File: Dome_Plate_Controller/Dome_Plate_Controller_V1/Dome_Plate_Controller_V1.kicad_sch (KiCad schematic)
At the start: 35 parts, among them J1 USB_B_Micro, J10 SERIAL_FU4, J11 SERIAL_FU3, J12 SERIAL_FU, J13 DB25_Female_MountingHoles, J14 DC-005-5A-2.0, J15 SERIAL_FU2, J2 DB25_Female_MountingHoles, J3 12VOUT, J4 SERIAL_RS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

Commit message: Working on new body control board
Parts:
- J13: value DB25_Female_MountingHoles -> DB25_Female_MagTag; LCSC C77833 -> C2834383
- J2: value DB25_Female_MountingHoles -> DB25_Male_SlipRing; footprint Connector_Dsub:DSUB-25_Female_Vertical_P2.77x2.84mm_MountingHoles -> Connector_Dsub:DSUB-25_Male_Vertical_P2.77x2.84mm_MountingHoles; LCSC C77833 -> C2834344
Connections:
- net RX_FU2: no longer U1.9 (IO33)
- net TX_FU2: no longer U1.8 (IO32)
- no-connect marks 30 -> 32
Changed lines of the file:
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@@
   (no_connect (at 69.85 73.66))
   (no_connect (at 87.63 187.96))
+  (no_connect (at 52.07 55.88))
   (no_connect (at 54.61 186.69))
   (no_connect (at 166.37 93.98))
@@
   (no_connect (at 95.25 53.34))
   (no_connect (at 135.89 97.79))
+  (no_connect (at 52.07 53.34))
   (no_connect (at 72.39 73.66))
   (no_connect (at 46.99 151.13))
@@
     )
   )
-  (global_label "TX_FU2" (shape input) (at 52.07 53.34 180) (fields_autoplaced)
-    (effects (font (size 1.27 1.27)) (justify right))
-    (property "Intersheet References" "${INTERSHEET_REFS}" (id 0) (at 42.8836 53.2606 0)
-      (effects (font (size 1.27 1.27)) (justify right) hide)
-    )
-  )
   (global_label "D+" (shape input) (at 135.89 92.71 0) (fields_autoplaced)
     (effects (font (size 1.27 1.27)) (justify left))
@@
     )
   )
-  (global_label "RX_FU2" (shape input) (at 96.52 78.74 0) (fields_autoplaced)
-    (effects (font (size 1.27 1.27)) (justify left))
-    (property "Intersheet References" "${INTERSHEET_REFS}" (id 0) (at 106.0088 78.6606 0)
-      (effects (font (size 1.27 1.27)) (justify left) hide)
-    )
-  )
   (global_label "RXD0" (shape input) (at 95.25 45.72 0) (fields_autoplaced)
     (effects (font (size 1.27 1.27)) (justify left))
@@
     (effects (font (size 1.27 1.27)) (justify right))
     (property "Intersheet References" "${INTERSHEET_REFS}" (id 0) (at 31.6706 101.4447 90)
-      (effects (font (size 1.27 1.27)) (justify right) hide)
-    )
-  )
-  (global_label "RX_FU2" (shape input) (at 52.07 55.88 180) (fields_autoplaced)
-    (effects (font (size 1.27 1.27)) (justify right))
-    (property "Intersheet References" "${INTERSHEET_REFS}" (id 0) (at 42.5812 55.8006 0)
       (effects (font (size 1.27 1.27)) (justify right) hide)
     )
@@
       (effects (font (size 1.27 1.27)) (justify left))
     )
-    (property "Value" "DB25_Female_MountingHoles" (id 1) (at 38.1 190.4999 0)
+    (property "Value" "DB25_Female_MagTag" (id 1) (at 38.1 190.4999 0)
       (effects (font (size 1.27 1.27)) (justify left))
     )
@@
       (effects (font (size 1.27 1.27)) hide)
     )
-    (property "LCSC" "C77833" (id 4) (at 54.61 151.13 0)
+    (property "LCSC" "C2834383" (id 4) (at 54.61 151.13 0)
       (effects (font (size 1.27 1.27)) hide)
     )
@@
       (effects (font (size 1.27 1.27)) (justify left))
     )
-    (property "Value" "DB25_Female_MountingHoles" (id 1) (at 73.66 191.7699 0)
-      (effects (font (size 1.27 1.27)) (justify left))
-    )
-    (property "Footprint" "Connector_Dsub:DSUB-25_Female_Vertical_P2.77x2.84mm_MountingHoles" (id 2) (at 87.63 152.4 0)
+    (property "Value" "DB25_Male_SlipRing" (id 1) (at 73.66 191.7699 0)
+      (effects (font (size 1.27 1.27)) (justify left))
+    )
+    (property "Footprint" "Connector_Dsub:DSUB-25_Male_Vertical_P2.77x2.84mm_MountingHoles" (id 2) (at 87.63 152.4 0)
       (effects (font (size 1.27 1.27)) hide)
     )
@@
       (effects (font (size 1.27 1.27)) hide)
     )
-    (property "LCSC" "C77833" (id 4) (at 87.63 152.4 0)
+    (property "LCSC" "C2834344" (id 4) (at 87.63 152.4 0)
       (effects (font (size 1.27 1.27)) hide)
     )
@@
     )
     (path "/6bc43df8-b439-4c10-945f-79b8aa8b1bbf"
-      (reference "J2") (unit 1) (value "DB25_Female_MountingHoles") (footprint "Connector_Dsub:DSUB-25_Female_Vertical_P2.77x2.84mm_MountingHoles")
+      (reference "J2") (unit 1) (value "DB25_Male_SlipRing") (footprint "Connector_Dsub:DSUB-25_Male_Vertical_P2.77x2.84mm_MountingHoles")
     )
     (path "/6e24a65e-6cc3-44ac-8a5b-662642e9396d"
@@
     )
     (path "/1eb3ffea-e932-409f-b4af-7d3f3af9d359"
-      (reference "J13") (unit 1) (value "DB25_Female_MountingHoles") (footprint "Connector_Dsub:DSUB-25_Female_Vertical_P2.77x2.84mm_MountingHoles")
+      (reference "J13") (unit 1) (value "DB25_Female_MagTag") (footprint "Connector_Dsub:DSUB-25_Female_Vertical_P2.77x2.84mm_MountingHoles")
     )
     (path "/b42cd28b-6776-49c3-af7d-a30bc22f7b3a"

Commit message: Added a lot since last check in
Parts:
- J4: value SERIAL_RS -> SERIAL_US
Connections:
- net D+: no longer J13.9
- net D-: no longer J13.21 (P21)
- net GND: no longer J13.8
- net VBUS: no longer J13.20 (P20)
- no-connect marks 32 -> 36
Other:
- moved on the sheet: J10, J11, J12, J15

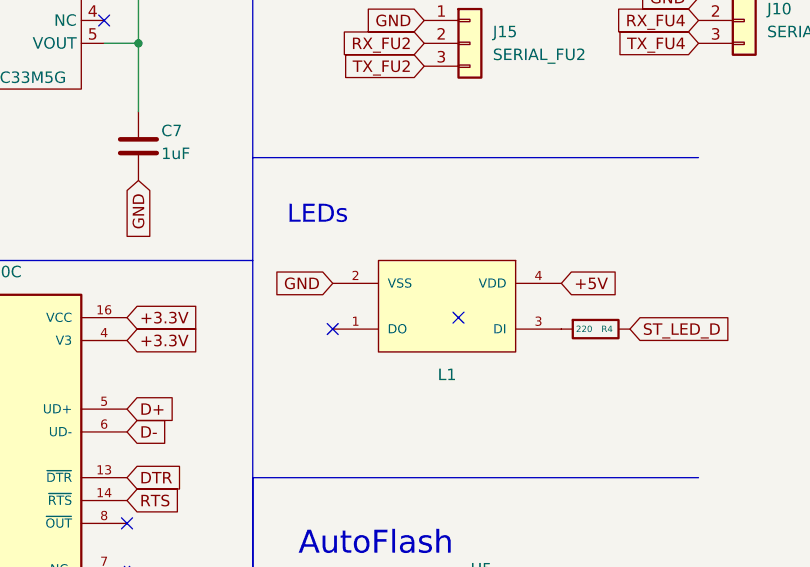
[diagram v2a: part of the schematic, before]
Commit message: added LED PCBs
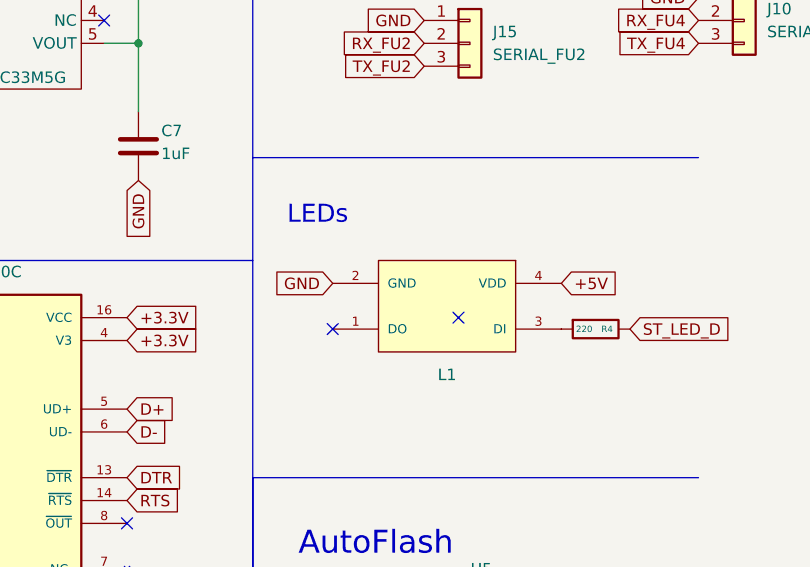
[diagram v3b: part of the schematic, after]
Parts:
- J13: LCSC C2834383 -> C2938621
- J14: LCSC C381116 -> C3010535
- J2: LCSC C2834344 -> C2984302
- L1: footprint Custom:WS2812B-2020 -> WS2812B-2020
